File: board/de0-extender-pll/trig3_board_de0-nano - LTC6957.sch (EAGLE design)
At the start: 92 parts, among them J12 4p-2.54, J13 BU-SMB-V, J17 2p-2.54, J23 2p-2.54, J24 2p-2.54, J3 4p-2.54, J32 2p-2.54, J33 2p-2.54, J34 2p-2.54, J38 2p-2.54, J39 2p-2.54, J42 2p-2.54, J43 2p-2.54, J5 2p-2.54, J6 2p-2.54, J7 4p-2.54, K15_R10P BU-SMB-V, K16_R10N BU-SMB-V, P11 BU-SMB-V, P15 BU-SMB-V, P16_R15N BU-SMB-V, P9 BU-SMB-V, T13_B20N BU-SMB-V, T9CLK_7N BU-SMB-V

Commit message: ltc6957 based board starting
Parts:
- added U1, U2: LTC6957HMS-2PBF, ltc6957-2:LTC6957HMS-2PBF
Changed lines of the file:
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@@
 <part name="R4" library="rcl" library_urn="urn:adsk.eagle:library:334" deviceset="R-US_" device="R0603" package3d_urn="urn:adsk.eagle:package:23555/3" value="130"/>
 <part name="R7" library="rcl" library_urn="urn:adsk.eagle:library:334" deviceset="R-US_" device="R0603" package3d_urn="urn:adsk.eagle:package:23555/3" value="100"/>
+<part name="U1" library="ltc6957-2" deviceset="LTC6957HMS-2PBF" device=""/>
+<part name="U2" library="ltc6957-2" deviceset="LTC6957HMS-2PBF" device=""/>
 </parts>
 <sheets>
@@
 <attribute name="VALUE" x="-19.558" y="151.13" size="1.778" layer="96" rot="R90"/>
 </instance>
+<instance part="U1" gate="A" x="-127" y="76.2" smashed="yes">
+<attribute name="NAME" x="-108.8644" y="85.3186" size="2.0828" layer="95" ratio="6" rot="SR0"/>
+<attribute name="VALUE" x="-109.4994" y="82.7786" size="2.0828" layer="96" ratio="6" rot="SR0"/>
+</instance>
+<instance part="U2" gate="A" x="-127" y="25.4" smashed="yes">
+<attribute name="NAME" x="-108.8644" y="34.5186" size="2.0828" layer="95" ratio="6" rot="SR0"/>
+<attribute name="VALUE" x="-109.4994" y="31.9786" size="2.0828" layer="96" ratio="6" rot="SR0"/>
+</instance>
 </instances>

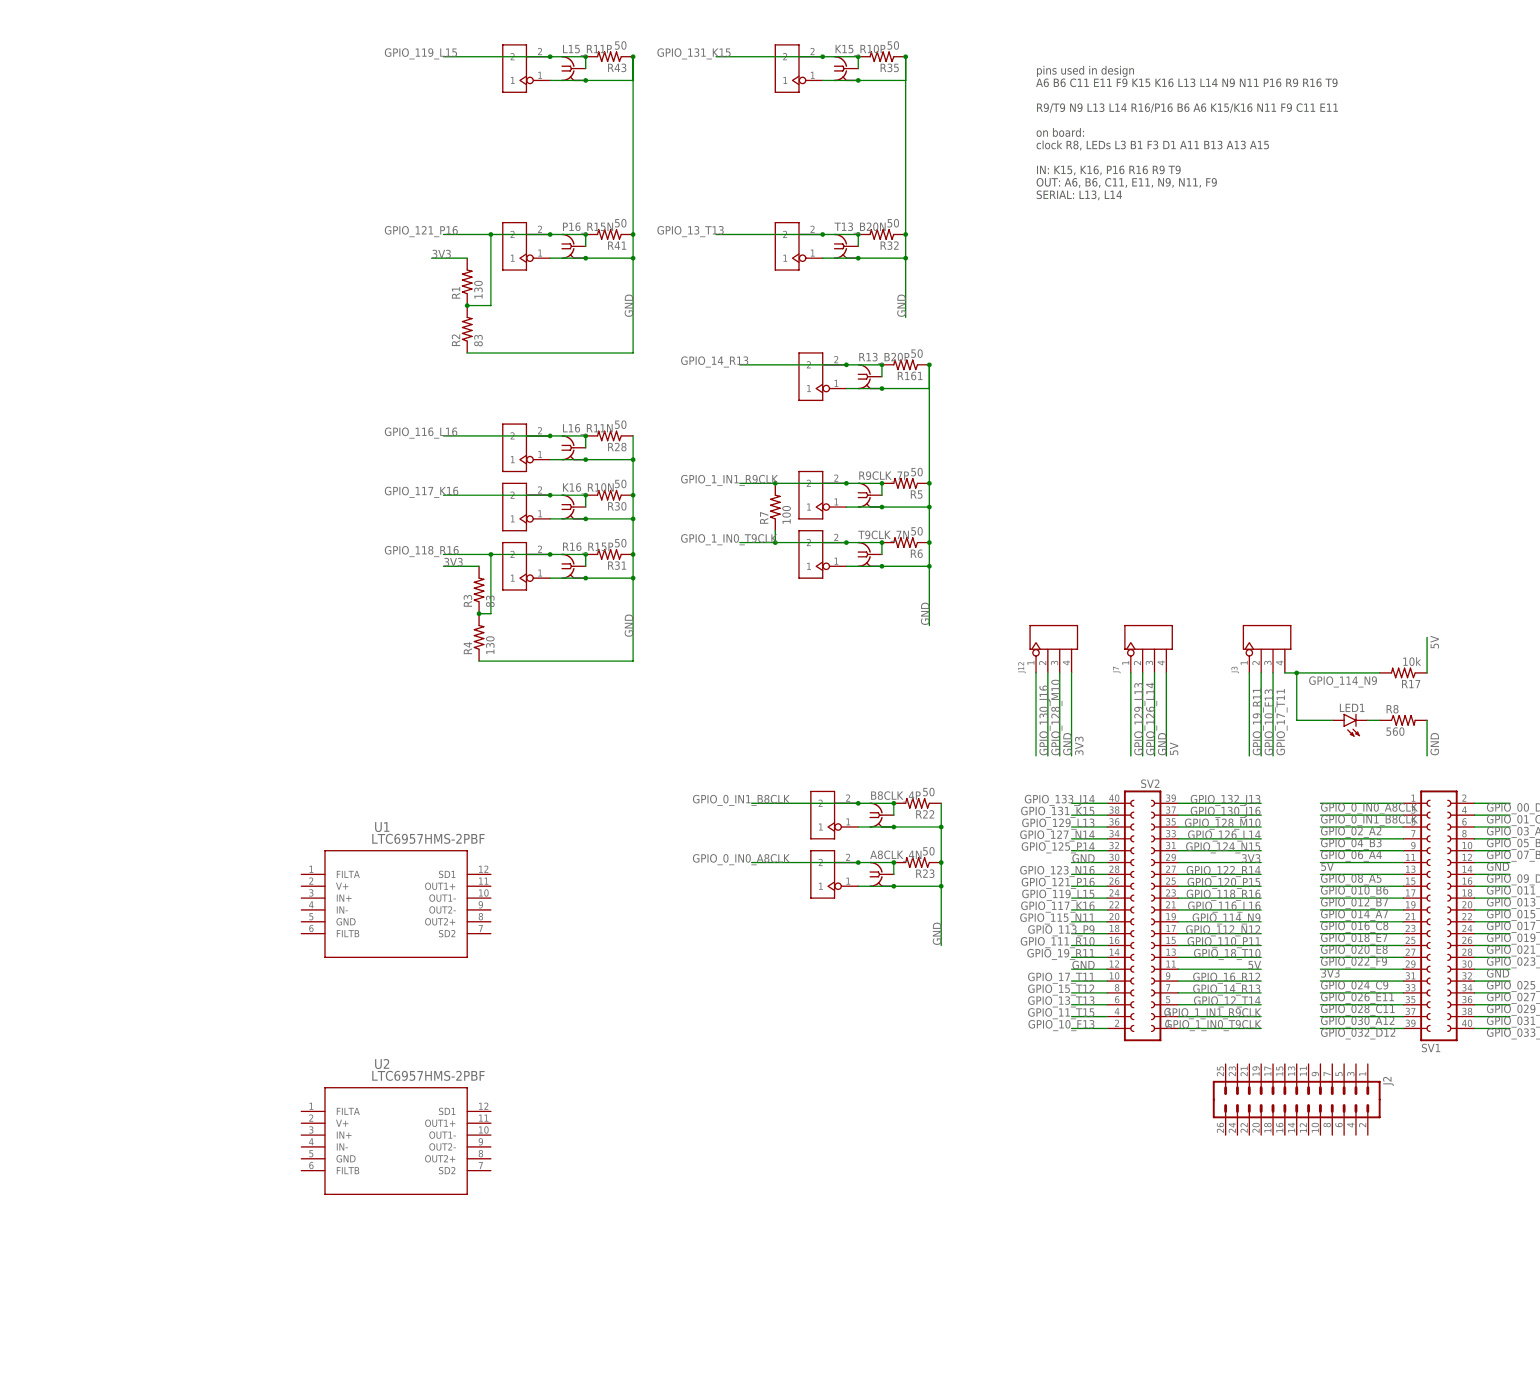
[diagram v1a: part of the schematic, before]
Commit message: fixed pecl termination
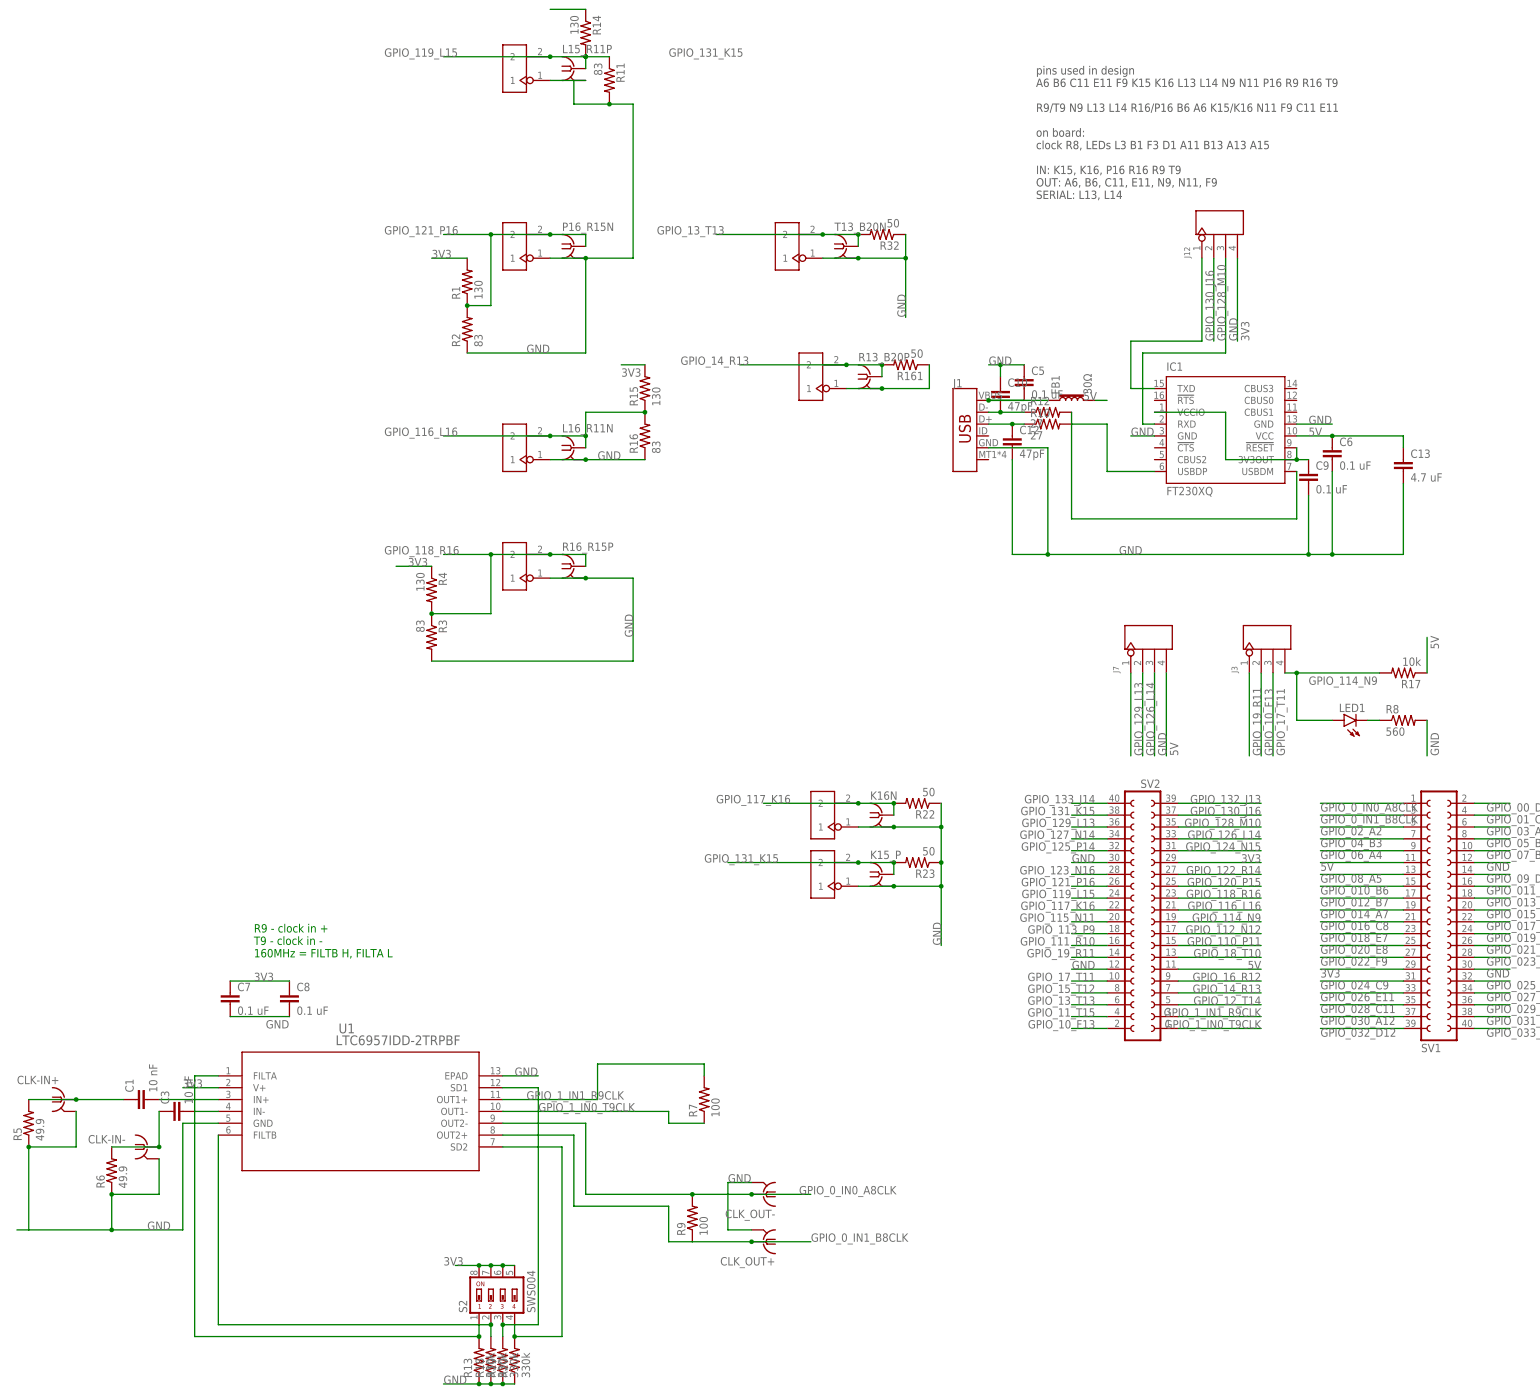
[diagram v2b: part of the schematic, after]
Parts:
- removed J2: (no value), SparkFun-Connectors:M13X22X13
- removed J33, J39, J5, J6: 2p-2.54, Seeed-Connector:DIP-BLACK-MALE-HEADER-VERT(2P-2.54)
- removed K15_R10P, K16_R10N, R9CLK_7P, T9CLK_7N: BU-SMB-V, con-coax:BU-SMB-V
- removed R28, R30, R31, R35, R41, R43: 50, SparkFun-Passives:RESISTORAXIAL-0.3
- removed U2: LTC6957HMS-2PBF, ltc6957-2:LTC6957HMS-2PBF
- added C1, C3: 10 nF, rcl:C-EUC0603
- added C10, C12: 47pF, rcl:C-EUC0603
- added C13: 4.7 uF, rcl:C-EUC0603
- added C5, C6, C7, C8, C9: 0.1 uF, rcl:C-EUC0603
- added CLK-IN+, CLK-IN-, CLK_OUT+, CLK_OUT-: BU-SMB-V, con-coax:BU-SMB-V
- added FB1: 30Ω, SparkFun-Coils:FERRITE_BEAD-0603-30OHM-100MHZ
- added IC1: FT230XQ, ftdichip:FT230XQ
- added J1: (no value), SparkFun-Connectors:USB_MICRO-B_SMT
- added R10, R12: 27, rcl:R-US_R0603
- added R11, R16: 83, rcl:R-US_R0603
- added R13, R18, R19, R20: 330k, rcl:R-US_R0603
- added R14, R15: 130, rcl:R-US_R0603
- added R9: 100, rcl:R-US_R0603
- added S2: SWS004, smd-special:SWS004
- C2, C4, C96: device SparkFun-Capacitors:CAP0805 -> SparkFun-Capacitors:CAP-0805
- LED1: LCSC_PART# (none) -> C84256
- R5, R6: value 50 -> 49.9; device SparkFun-Passives:RESISTORAXIAL-0.3 -> rcl:R-US_R0603; LCSC_PART# (none) -> C23185
- R7: LCSC_PART# (none) -> C22775
- U1: value LTC6957HMS-2PBF -> LTC6957IDD-2TRPBF; device ltc6957-2:LTC6957HMS-2PBF -> ltc6957-2:LTC6957IDD-2TRPBF
- renumbered A8CLK_4N to K15_P, B8CLK_4P to K16N
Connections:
- new net N$1: J17.1, R13_B20P.2, R161.1
- new net N$11: C10.2, J1.D-, R12.1
- new net N$12: IC1.USBDP, R10.2
- new net N$13: IC1.USBDM, R12.2
- new net N$14: C9.1, IC1.!RESET, IC1.3V3OUT, IC1.VCCIO
- new net N$15: R13.2, S2.1, U1.FILTA
- new net N$16: R18.2, S2.2, U1.FILTB
- new net N$17: R19.2, S2.3, U1.SD1
- new net N$18: R20.2, S2.4, U1.SD2
- new net N$2: C1.1, CLK-IN+.1, R5.2
- new net N$3: C3.1, CLK-IN-.1, R6.2
- new net N$4: C1.2, U1.IN+
- new net N$5: C3.2, U1.IN-
- new net N$6: C5.2, FB1.1, J1.VBUS
- new net N$7: C12.1, J1.D+, R10.1
- net 3V3: now also C7.1, C8.1, R14.1, R15.2, R4.1, S2.5, S2.6, S2.7, S2.8, U1.V+; no longer R3.2
- net 5V: now also C13.1, C6.1, FB1.2, IC1.VCC
- net GND: now also C10.1, C12.2, C13.2, C5.1, C6.2, C7.2, C8.2, C9.2, CLK-IN+.2, CLK-IN-.2, CLK_OUT+.2, CLK_OUT-.2, IC1.GND, IC1.GND@1, IC1.RXD, J1.GND, R11.2, R13.1, R16.1, R18.1, R19.1, R20.1, R3.2, U1.EPAD, U1.GND; no longer J17.1, J33.1, J39.1, J5.1, J6.1, K15_R10P.2, K16_R10N.2, R13_B20P.2, R161.1, R28.1, R30.1, R31.1, R35.1, R4.1, R41.1, R43.1, R9CLK_7P.2, T9CLK_7N.2
- net GPIO_0_IN0_A8CLK: now also CLK_OUT-.1, R9.2, U1.OUT2-; no longer J24.2, K15_P.1, R23.2
- net GPIO_0_IN1_B8CLK: now also CLK_OUT+.1, R9.1, U1.OUT2+; no longer J23.2, K16N.1, R22.2
- net GPIO_116_L16: now also R15.1, R16.2; no longer R28.2
- net GPIO_117_K16: now also J23.2, K16N.1, R22.2; no longer J33.2, K16_R10N.1, R30.2
- net GPIO_118_R16: no longer R31.2
- net GPIO_119_L15: now also R11.1, R14.2; no longer R43.2
- net GPIO_121_P16: no longer R41.2
- net GPIO_130_J16: now also IC1.TXD
- net GPIO_131_K15: now also J24.2, K15_P.1, R23.2; no longer J39.2, K15_R10P.1, R35.2
- net GPIO_1_IN0_T9CLK: now also U1.OUT1-; no longer J6.2, R6.2, T9CLK_7N.1
- net GPIO_1_IN1_R9CLK: now also U1.OUT1+; no longer J5.2, R5.2, R9CLK_7P.1
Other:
- note added: "R9 - clock in + T9 - clock in - 160MHz = FILTB H, FILTA L"
- moved on the sheet: J12, R3, R4, R5, R6, R7

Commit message: more work on board
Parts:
- VSLUE5, VSLUE7, VSLUE9: value SN74ACT244DW -> SN74LVTH244ARGYR; device SN74ACT244DW:SN74ACT244DW -> sn74lvth244argyr:SN74LVTH244ARGYR
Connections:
- net 3V3: now also C2.2, C4.2, C96.2, VSLUE5.VCC, VSLUE7.VCC, VSLUE9.VCC
- net 5V: no longer C2.2, C4.2, C96.2, VSLUE5.VCC, VSLUE7.VCC, VSLUE9.VCC
- net GND: now also VSLUE5.EPAD, VSLUE7.EPAD, VSLUE9.EPAD

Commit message: ready to autoroute
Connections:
- net 3V3: now also R17.1
- net 5V: no longer R17.1
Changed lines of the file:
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@@
 </variantdefs>
 <classes>
-<class number="0" name="default" width="0.254" drill="0">
+<class number="0" name="default" width="0" drill="0">
 </class>
-<class number="1" name="power" width="0.762" drill="0">
+<class number="1" name="power" width="0" drill="0">
 </class>
 <class number="2" name="used_pins" width="0" drill="0">
@@
 <net name="5V" class="1">
 <segment>
-<pinref part="R17" gate="G$1" pin="1"/>
-<wire x1="116.84" y1="119.38" x2="116.84" y2="127" width="0.1524" layer="91"/>
-<label x="119.38" y="124.46" size="1.778" layer="95" rot="R90"/>
-</segment>
-<segment>
 <pinref part="SV1" gate="G$1" pin="11"/>
 <wire x1="111.76" y1="78.74" x2="93.98" y2="78.74" width="0.1524" layer="91"/>
@@
 <label x="279.4" y="243.84" size="1.778" layer="95"/>
 </segment>
-</net>
+<segment>
+<pinref part="R17" gate="G$1" pin="1"/>
+<wire x1="116.84" y1="119.38" x2="124.46" y2="119.38" width="0.1524" layer="91"/>
+<label x="119.38" y="119.38" size="1.778" layer="95"/>
+</segment>
+</net>

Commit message: autoroute attempt 2
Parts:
- removed OJ45, OJ46, OJ47, OJ48, OJ61, OJ62, OJ63, OJ64, OJ77, OJ78, OJ79, OJ80: 2p-2.54, Seeed-Connector:DIP-BLACK-MALE-HEADER-VERT(2P-2.54)
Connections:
- net GND: no longer OJ45.2, OJ46.2, OJ47.2, OJ48.2, OJ61.2, OJ62.2, OJ63.2, OJ64.2, OJ77.2, OJ78.2, OJ79.2, OJ80.2
- net GPIO_010_B6: no longer OJ47.1
- net GPIO_011_A6: no longer OJ48.1
- net GPIO_018_E7: no longer OJ64.1
- net GPIO_022_F9: no longer OJ62.1
- net GPIO_026_E11: no longer OJ79.1
- net GPIO_028_C11: no longer OJ78.1
- net GPIO_110_P11: no longer OJ80.1
- net GPIO_113_P9: no longer OJ45.1
- net GPIO_115_N11: no longer OJ46.1
- net GPIO_120_P15: no longer OJ61.1
- net GPIO_132_J13: no longer OJ77.1
- net GPIO_23_C16: no longer OJ63.1

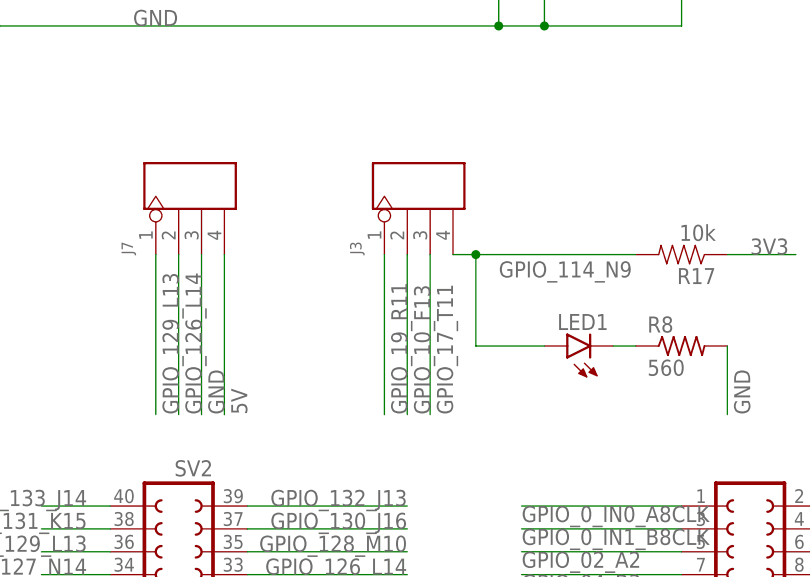
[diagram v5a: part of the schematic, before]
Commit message: removed unnecessary header
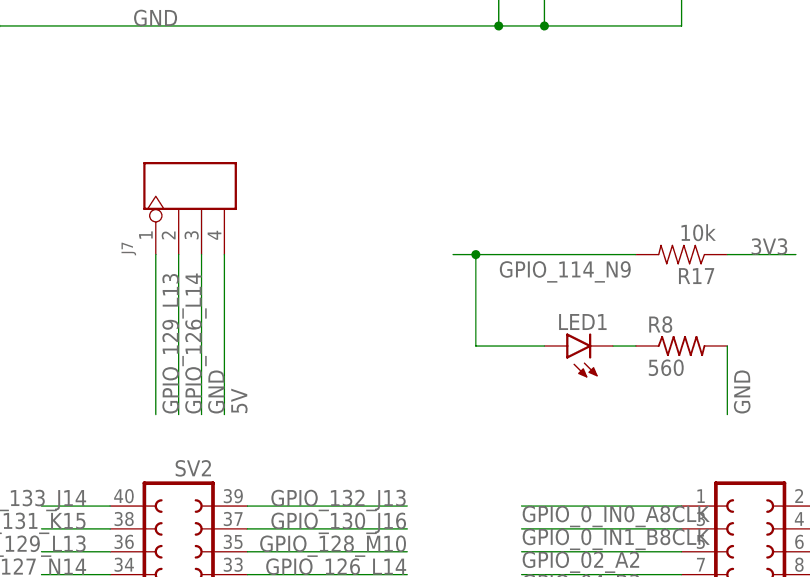
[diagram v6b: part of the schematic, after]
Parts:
- removed J3: 4p-2.54, Seeed-Connector:DIP-BLACK-FEMALE-HEADER-VERT(4P-2.54)
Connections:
- net GPIO_10_F13: no longer J3.P$2
- net GPIO_114_N9: no longer J3.P$4
- net GPIO_17_T11: no longer J3.P$3
- net GPIO_19_R11: no longer J3.P$1
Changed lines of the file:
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@@
 <part name="J38" library="Seeed-Connector" library_urn="urn:adsk.eagle:library:478" deviceset="DIP-BLACK-MALE-HEADER-VERT(2P-2.54)" device="" package3d_urn="urn:adsk.eagle:package:33132/1" value="2p-2.54"/>
 <part name="R32" library="SparkFun-Passives" deviceset="RESISTOR" device="AXIAL-0.3" value="50"/>
-<part name="J3" library="Seeed-Connector" library_urn="urn:adsk.eagle:library:478" deviceset="DIP-BLACK-FEMALE-HEADER-VERT(4P-2.54)" device="" package3d_urn="urn:adsk.eagle:package:33137/1" value="4p-2.54"/>
 <part name="LED1" library="led" library_urn="urn:adsk.eagle:library:259" deviceset="LED" device="CHIP-LED0805" package3d_urn="urn:adsk.eagle:package:15818/2" value="red">
 <attribute name="LCSC_PART#" value="C84256"/>
@@
 <attribute name="VALUE" x="3.81" y="216.662" size="1.778" layer="96" rot="R180"/>
 </instance>
-<instance part="J3" gate="G$1" x="82.55" y="127" smashed="yes" rot="R90">
-<attribute name="NAME" x="76.2" y="119.38" size="1.27" layer="95" ratio="10" rot="R90"/>
-</instance>
 <instance part="LED1" gate="G$1" x="99.06" y="109.22" smashed="yes" rot="R90">
 <attribute name="NAME" x="103.632" y="112.776" size="1.778" layer="95" rot="R180"/>
@@
 <label x="45.72" y="43.18" size="1.778" layer="95" rot="MR0"/>
 </segment>
-<segment>
-<pinref part="J3" gate="G$1" pin="P$2"/>
-<wire x1="81.28" y1="119.38" x2="81.28" y2="101.6" width="0.1524" layer="91"/>
-<label x="83.82" y="101.6" size="1.778" layer="95" rot="R90"/>
-</segment>
 </net>
 <net name="GPIO_11_T15" class="0">
@@
 <label x="45.72" y="53.34" size="1.778" layer="95" rot="MR0"/>
 </segment>
-<segment>
-<pinref part="J3" gate="G$1" pin="P$3"/>
-<wire x1="83.82" y1="119.38" x2="83.82" y2="101.6" width="0.1524" layer="91"/>
-<label x="86.36" y="101.6" size="1.778" layer="95" rot="R90"/>
-</segment>
 </net>
 <net name="GPIO_19_R11" class="0">
@@
 <wire x1="48.26" y1="58.42" x2="40.64" y2="58.42" width="0.1524" layer="91"/>
 <label x="45.72" y="58.42" size="1.778" layer="95" rot="MR0"/>
-</segment>
-<segment>
-<pinref part="J3" gate="G$1" pin="P$1"/>
-<wire x1="78.74" y1="119.38" x2="78.74" y2="101.6" width="0.1524" layer="91"/>
-<label x="81.28" y="101.6" size="1.778" layer="95" rot="R90"/>
 </segment>
 </net>
@@
 <wire x1="106.68" y1="119.38" x2="88.9" y2="119.38" width="0.1524" layer="91"/>
 <label x="91.44" y="116.84" size="1.778" layer="95"/>
-<pinref part="J3" gate="G$1" pin="P$4"/>
 <pinref part="LED1" gate="G$1" pin="A"/>
 <wire x1="88.9" y1="119.38" x2="86.36" y2="119.38" width="0.1524" layer="91"/>
